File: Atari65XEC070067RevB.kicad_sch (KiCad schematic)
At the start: 338 parts, among them J1 SIO, J2 MONITOR, J5 JOY1, J6 JOY1, J7 DIN-7, J8 KEYBOARD, Q1 2N3904, Q2 2N3904, Q3 2N3904, Q4 2N3904, Q5 2N3904, Q6 2N3904, Q7 MPSA55, SW1 SW_SPDT, U1 LM358, U10 4164, U11 4164, U12 4164, U13 4164, U14 4164, U15 4164, U16 4164, U17 C014889/GTIA, U18 74LS08, U19 NE555P, U2 74LS138, U20 4050, U21 74LS74, U22 C012294/POKEY, U23 C014795 PIA/6520, U24 4051, U25 4051, U26 4164, U27 4164, U28 4164, U29 4164, U3 MMU, U30 4164, U31 4164, U32 4164, U33 4164, U34 MMMU, U35 74LS95, U4 BASIC, U5 OS ROM, U6 CO14806/SALLY, U7 C021698/ANTIC, U8 C061991/FREDDIE, U9 4164, Y2 4.33618MHz

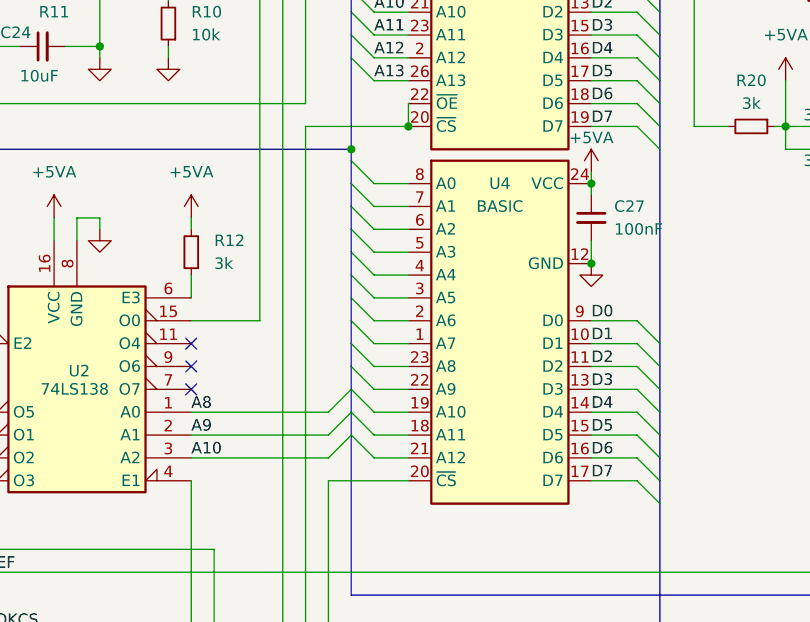
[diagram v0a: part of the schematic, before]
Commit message: fix ROM positions
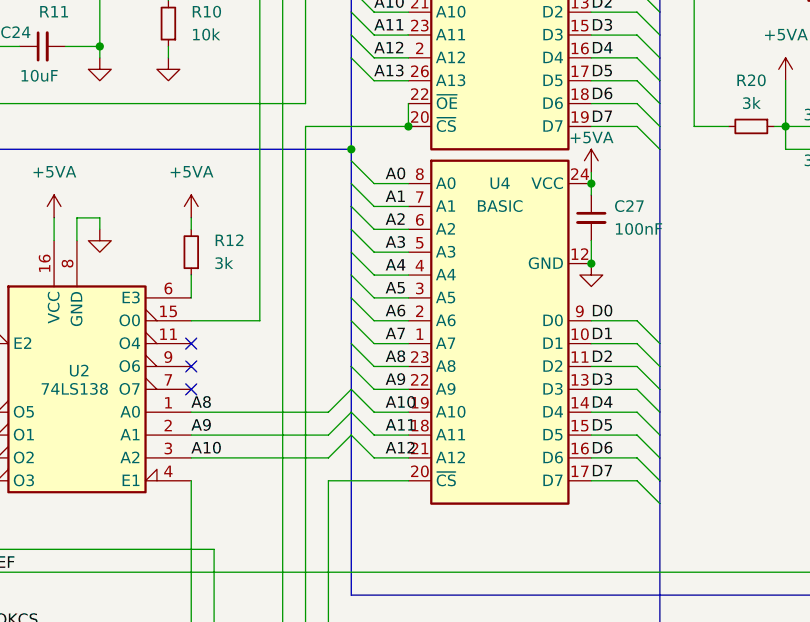
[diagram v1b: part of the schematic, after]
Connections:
- net A0: now also U4.8 (A0)
- net A1: now also U4.7 (A1)
- net A10: now also U4.19 (A10)
- net A11: now also U4.18 (A11)
- net A12: now also U4.21 (A12)
- net A2: now also U4.6 (A2)
- net A3: now also U4.5 (A3)
- net A4: now also U4.4 (A4)
- net A5: now also U4.3 (A5)
- net A6: now also U4.2 (A6)
- net A7: now also U4.1 (A7)
- net A8: now also U4.23 (A8)
- net A9: now also U4.22 (A9)
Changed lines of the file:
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@@
+		)
+	)
+	(label "A1"
+		(at 132.08 160.02 0)
+		(effects
+			(font
+				(size 1.27 1.27)
+			)
+			(justify left bottom)
 		)
 	)
@@
 		)
 	)
+	(label "A5"
+		(at 132.08 170.18 0)
+		(effects
+			(font
+				(size 1.27 1.27)
+			)
+			(justify left bottom)
+		)
+	)
 	(label "A4"
 		(at 203.2 95.25 0)
@@
 		)
 	)
+	(label "A3"
+		(at 132.08 165.1 0)
+		(effects
+			(font
+				(size 1.27 1.27)
+			)
+			(justify left bottom)
+		)
+	)
 	(label "D4"
 		(at 154.94 182.88 0)
@@
 		)
 	)
+	(label "A12"
+		(at 132.08 187.96 0)
+		(effects
+			(font
+				(size 1.27 1.27)
+			)
+			(justify left bottom)
+		)
+	)
 	(label "P2"
 		(at 461.01 351.79 0)
@@
 		)
 	)
+	(label "A10"
+		(at 132.08 182.88 0)
+		(effects
+			(font
+				(size 1.27 1.27)
+			)
+			(justify left bottom)
+		)
+	)
 	(label "D6"
 		(at 361.95 318.77 180)
@@
 		)
 	)
+	(label "A6"
+		(at 132.08 172.72 0)
+		(effects
+			(font
+				(size 1.27 1.27)
+			)
+			(justify left bottom)
+		)
+	)
 	(label "A12"
 		(at 130.81 143.51 0)
@@
 		)
 	)
+	(label "A0"
+		(at 132.08 157.48 0)
+		(effects
+			(font
+				(size 1.27 1.27)
+			)
+			(justify left bottom)
+		)
+	)
 	(label "PB7"
 		(at 85.09 228.6 0)
@@
 		)
 	)
+	(label "A2"
+		(at 132.08 162.56 0)
+		(effects
+			(font
+				(size 1.27 1.27)
+			)
+			(justify left bottom)
+		)
+	)
 	(label "A15"
 		(at 203.2 123.19 0)
@@
 		)
 	)
+	(label "A8"
+		(at 132.08 177.8 0)
+		(effects
+			(font
+				(size 1.27 1.27)
+			)
+			(justify left bottom)
+		)
+	)
 	(label "A0"
 		(at 130.81 113.03 0)
@@
 		)
 	)
+	(label "A7"
+		(at 132.08 175.26 0)
+		(effects
+			(font
+				(size 1.27 1.27)
+			)
+			(justify left bottom)
+		)
+	)
 	(label "S0"
 		(at 299.72 107.95 0)
@@
 		)
 	)
+	(label "A11"
+		(at 132.08 185.42 0)
+		(effects
+			(font
+				(size 1.27 1.27)
+			)
+			(justify left bottom)
+		)
+	)
 	(label "D5"
 		(at 285.75 259.08 0)
@@
 		)
 	)
+	(label "A9"
+		(at 132.08 180.34 0)
+		(effects
+			(font
+				(size 1.27 1.27)
+			)
+			(justify left bottom)
+		)
+	)
 	(label "A15"
 		(at 82.55 323.85 180)
@@
 		)
 	)
+	(label "A4"
+		(at 132.08 167.64 0)
+		(effects
+			(font
+				(size 1.27 1.27)
+			)
+			(justify left bottom)
+		)
+	)

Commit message: progress routing
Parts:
- L37: footprint Inductor_THT:L_Axial_L7.0mm_D3.3mm_P12.70mm_Horizontal_Fastron_MICC -> Library:R_Axial_L9.0mm_D2.7mm_P12.70mm_Horizontal
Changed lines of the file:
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@@
 			)
 		)
-		(property "Footprint" "Inductor_THT:L_Axial_L7.0mm_D3.3mm_P12.70mm_Horizontal_Fastron_MICC"
+		(property "Footprint" "Library:R_Axial_L9.0mm_D2.7mm_P12.70mm_Horizontal"
 			(at 247.65 228.6 0)
 			(effects

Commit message: fix phi2 wiring
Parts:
- L8: footprint Inductor_THT:L_Axial_L7.0mm_D3.3mm_P12.70mm_Horizontal_Fastron_MICC -> Library:R_Axial_L9.0mm_D2.7mm_P12.70mm_Horizontal
- renumbered R20 to R19, R19 to R20
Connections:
- net BO2: no longer U34.19 (O2), U8.5 (O2)
- net at Y2.1: now also C111.1, L8.1, R71.1; no longer C59.2
- net at U23.12 (PB2), U34.3 (BA14): now also R23.2; no longer R25.2
- net at U23.13 (PB3), U34.4 (BA15): now also R25.2; no longer R23.2
- net at R20.1, U18.1: now also U34.19 (O2), U6.39 (O2), U8.5 (O2)
- new net: C59.2, Y2.2
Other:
- moved on the sheet: R13, R20

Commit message: update fills and footprints
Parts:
- J8: footprint (none) -> Library:KEYBOARD
- Q1, Q2, Q3, Q4, Q5, Q6, Q7: footprint PCM_Package_TO_SOT_THT_AKL:TO-92_Inline_Wide_EBC -> Library:TO-92L_Inline_Wide
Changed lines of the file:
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@@
 			)
 		)
-		(property "Footprint" "PCM_Package_TO_SOT_THT_AKL:TO-92_Inline_Wide_EBC"
+		(property "Footprint" "Library:TO-92L_Inline_Wide"
 			(at 212.09 382.27 0)
 			(effects
@@
 			)
 		)
-		(property "Footprint" "PCM_Package_TO_SOT_THT_AKL:TO-92_Inline_Wide_EBC"
+		(property "Footprint" "Library:TO-92L_Inline_Wide"
 			(at 398.78 118.11 0)
 			(effects
@@
 			)
 		)
-		(property "Footprint" "PCM_Package_TO_SOT_THT_AKL:TO-92_Inline_Wide_EBC"
+		(property "Footprint" "Library:TO-92L_Inline_Wide"
 			(at 391.16 72.39 0)
 			(effects
@@
 			)
 		)
-		(property "Footprint" "PCM_Package_TO_SOT_THT_AKL:TO-92_Inline_Wide_EBC"
+		(property "Footprint" "Library:TO-92L_Inline_Wide"
 			(at 471.17 107.95 0)
 			(effects
@@
 			)
 		)
-		(property "Footprint" "PCM_Package_TO_SOT_THT_AKL:TO-92_Inline_Wide_EBC"
+		(property "Footprint" "Library:TO-92L_Inline_Wide"
 			(at 190.5 374.65 0)
 			(effects
@@
 			)
 		)
-		(property "Footprint" ""
+		(property "Footprint" "Library:KEYBOARD"
 			(at 497.84 309.88 0)
 			(effects
@@
 			)
 		)
-		(property "Footprint" "PCM_Package_TO_SOT_THT_AKL:TO-92_Inline_Wide_EBC"
+		(property "Footprint" "Library:TO-92L_Inline_Wide"
 			(at 355.6 153.67 0)
 			(effects
@@
 			)
 		)
-		(property "Footprint" "PCM_Package_TO_SOT_THT_AKL:TO-92_Inline_Wide_EBC"
+		(property "Footprint" "Library:TO-92L_Inline_Wide"
 			(at 283.21 171.45 0)
 			(effects

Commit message: refine board definition
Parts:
- added H1, H2: MountingHole, Library:Cutout, symbol Mechanical:MountingHole
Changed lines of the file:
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@@
 	)
 	(symbol
+		(lib_id "Mechanical:MountingHole")
+		(at 17.78 363.22 0)
+		(unit 1)
+		(exclude_from_sim yes)
+		(in_bom no)
+		(on_board yes)
+		(dnp no)
+		(fields_autoplaced yes)
+		(property "Reference" "H1"
+			(at 20.32 361.9499 0)
+			(effects
+				(font
+					(size 1.27 1.27)
+				)
+				(justify left)
+			)
+		)
+		(property "Value" "MountingHole"
+			(at 20.32 364.4899 0)
+			(effects
+				(font
+					(size 1.27 1.27)
+				)
+				(justify left)
+			)
+		)
+		(property "Footprint" "Library:Cutout"
+			(at 17.78 363.22 0)
+			(effects
+				(font
+					(size 1.27 1.27)
+				)
+				(hide yes)
+			)
+		)
+		(property "Datasheet" "~"
+			(at 17.78 363.22 0)
+			(effects
+				(font
+					(size 1.27 1.27)
+				)
+				(hide yes)
+			)
+		)
+		(property "Description" "Mounting Hole without connection"
+			(at 17.78 363.22 0)
+			(effects
+				(font
+					(size 1.27 1.27)
+				)
+				(hide yes)
+			)
+		)
+		(instances
+			(project ""
+				(path "/87d66ada-8337-4a7e-bc00-d889029d79b8"
+					(reference "H1")
+					(unit 1)
+				)
+			)
+		)
+	)
+	(symbol
 		(lib_id "power:GND")
 		(at 237.49 317.5 0)
@@
 					(unit 1)
 				)
+			)
+		)
+	)
+	(symbol
+		(lib_id "Mechanical:MountingHole")
+		(at 17.78 369.57 0)
+		(unit 1)
+		(exclude_from_sim yes)
+		(in_bom no)
+		(on_board yes)
+		(dnp no)
+		(fields_autoplaced yes)
+		(property "Reference" "H2"
+			(at 20.32 368.2999 0)
+			(effects
+				(font
+					(size 1.27 1.27)
+				)
+				(justify left)
+			)
+		)
+		(property "Value" "MountingHole"
+			(at 20.32 370.8399 0)
+			(effects
+				(font
+					(size 1.27 1.27)
+				)
+				(justify left)
+			)
+		)
+		(property "Footprint" "Library:Cutout"
+			(at 17.78 369.57 0)
+			(effects
+				(font
+					(size 1.27 1.27)
+				)
+				(hide yes)
+			)
+		)
+		(property "Datasheet" "~"
+			(at 17.78 369.57 0)
+			(effects
+				(font
+					(size 1.27 1.27)
+				)
+				(hide yes)
+			)
+		)
+		(property "Description" "Mounting Hole without connection"
+			(at 17.78 369.57 0)
+			(effects
+				(font
+					(size 1.27 1.27)
+				)
+				(hide yes)
+			)
+		)
+		(instances
+			(project "Atari65XEC070067RevB"
+				(path "/87d66ada-8337-4a7e-bc00-d889029d79b8"
+					(reference "H2")
+					(unit 1)
+				)

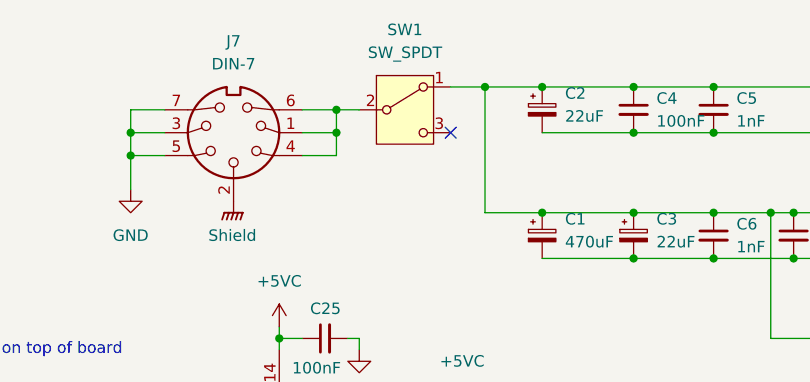
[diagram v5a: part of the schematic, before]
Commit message: place power circuit components
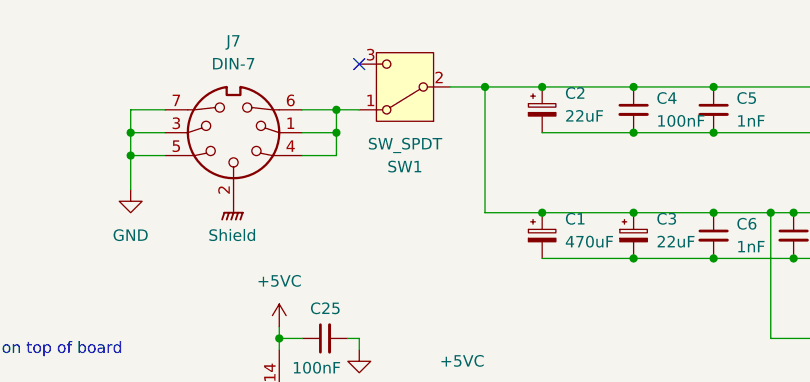
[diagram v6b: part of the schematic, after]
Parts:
- C1: footprint Capacitor_THT:CP_Radial_D8.0mm_P5.00mm -> Capacitor_THT:CP_Radial_D10.0mm_P5.00mm
- C10, C2, C3: footprint Capacitor_THT:CP_Radial_D8.0mm_P5.00mm -> Capacitor_THT:CP_Axial_L11.0mm_D5.0mm_P18.00mm_Horizontal
- J7: footprint (none) -> Library:CUI_SDS-70J
- L1, L2, L3: footprint Inductor_THT:L_Axial_L7.0mm_D3.3mm_P12.70mm_Horizontal_Fastron_MICC -> Library:R_Axial_L9.0mm_D2.7mm_P12.70mm_Horizontal
- SW1: footprint (none) -> Library:PowerSwitch
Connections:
- net at C1.1, C2.1, C3.1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: now also SW1.2 (B); no longer SW1.1 (A)
- net at J7.1, J7.4, J7.6: now also SW1.1 (A); no longer SW1.2 (B)
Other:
- moved on the sheet: SW1
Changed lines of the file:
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@@
 	)
 	(no_connect
-		(at 88.9 27.94)
+		(at 78.74 20.32)
 	)
 	(no_connect
@@
 			)
 		)
-		(property "Footprint" "Capacitor_THT:CP_Radial_D8.0mm_P5.00mm"
+		(property "Footprint" "Capacitor_THT:CP_Axial_L11.0mm_D5.0mm_P18.00mm_Horizontal"
 			(at 109.22 39.37 0)
 			(effects
@@
 			)
 		)
-		(property "Footprint" "Inductor_THT:L_Axial_L7.0mm_D3.3mm_P12.70mm_Horizontal_Fastron_MICC"
+		(property "Footprint" "Library:R_Axial_L9.0mm_D2.7mm_P12.70mm_Horizontal"
 			(at 133.35 22.86 0)
 			(effects
@@
 			)
 		)
-		(property "Footprint" "Capacitor_THT:CP_Radial_D8.0mm_P5.00mm"
+		(property "Footprint" "Capacitor_THT:CP_Radial_D10.0mm_P5.00mm"
 			(at 99.06 39.37 0)
 			(effects
@@
 			)
 		)
-		(property "Footprint" "Capacitor_THT:CP_Radial_D8.0mm_P5.00mm"
+		(property "Footprint" "Capacitor_THT:CP_Axial_L11.0mm_D5.0mm_P18.00mm_Horizontal"
 			(at 142.24 53.34 0)
 			(effects
@@
 			)
 		)
-		(property "Footprint" "Inductor_THT:L_Axial_L7.0mm_D3.3mm_P12.70mm_Horizontal_Fastron_MICC"
+		(property "Footprint" "Library:R_Axial_L9.0mm_D2.7mm_P12.70mm_Horizontal"
 			(at 133.35 50.8 0)
 			(effects
@@
 	(symbol
 		(lib_id "Switch:SW_SPDT")
-		(at 83.82 25.4 0)
+		(at 83.82 22.86 180)
 		(unit 1)
 		(exclude_from_sim no)
@@
 		(fields_autoplaced yes)
 		(property "Reference" "SW1"
-			(at 83.82 16.51 0)
+			(at 83.82 31.75 0)
 			(effects
 				(font
@@
 		)
 		(property "Value" "SW_SPDT"
-			(at 83.82 19.05 0)
+			(at 83.82 29.21 0)
 			(effects
 				(font
@@
 			)
 		)
-		(property "Footprint" ""
-			(at 83.82 25.4 0)
+		(property "Footprint" "Library:PowerSwitch"
+			(at 83.82 22.86 0)
 			(effects
 				(font
@@
 		)
 		(property "Datasheet" "~"
-			(at 83.82 33.02 0)
+			(at 83.82 15.24 0)
 			(effects
 				(font
@@
 		)
 		(property "Description" "Switch, single pole double throw"
-			(at 83.82 25.4 0)
+			(at 83.82 22.86 0)
 			(effects
 				(font
@@
 			)
 		)
-		(property "Footprint" ""
+		(property "Footprint" "Library:CUI_SDS-70J"
 			(at 64.77 27.94 0)
 			(effects
@@
 			)
 		)
-		(property "Footprint" "Inductor_THT:L_Axial_L7.0mm_D3.3mm_P12.70mm_Horizontal_Fastron_MICC"
+		(property "Footprint" "Library:R_Axial_L9.0mm_D2.7mm_P12.70mm_Horizontal"
 			(at 133.35 36.83 0)
 			(effects
@@
 			)
 		)
-		(property "Footprint" "Capacitor_THT:CP_Radial_D8.0mm_P5.00mm"
+		(property "Footprint" "Capacitor_THT:CP_Axial_L11.0mm_D5.0mm_P18.00mm_Horizontal"
 			(at 99.06 25.4 0)
 			(effects

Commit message: revise ram chip positions
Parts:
- C113, C114, C115, C116, C117, C118, C119, C120, C34, C35, C36, C37, C38, C39, C40, C41: footprint Library:C_Axial_L3.8mm_D2.6mm_P10.16mm_Horizontal -> Library:C_Axial_L3.8mm_D2.6mm_P8.89mm_Horizontal
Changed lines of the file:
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@@
 			)
 		)
-		(property "Footprint" "Library:C_Axial_L3.8mm_D2.6mm_P10.16mm_Horizontal"
+		(property "Footprint" "Library:C_Axial_L3.8mm_D2.6mm_P8.89mm_Horizontal"
 			(at 214.63 313.69 0)
 			(effects
@@
 			)
 		)
-		(property "Footprint" "Library:C_Axial_L3.8mm_D2.6mm_P10.16mm_Horizontal"
+		(property "Footprint" "Library:C_Axial_L3.8mm_D2.6mm_P8.89mm_Horizontal"
 			(at 285.75 313.69 0)
 			(effects
@@
 			)
 		)
-		(property "Footprint" "Library:C_Axial_L3.8mm_D2.6mm_P10.16mm_Horizontal"
+		(property "Footprint" "Library:C_Axial_L3.8mm_D2.6mm_P8.89mm_Horizontal"
 			(at 207.01 313.69 0)
 			(effects
@@
 			)
 		)
-		(property "Footprint" "Library:C_Axial_L3.8mm_D2.6mm_P10.16mm_Horizontal"
+		(property "Footprint" "Library:C_Axial_L3.8mm_D2.6mm_P8.89mm_Horizontal"
 			(at 184.15 313.69 0)
 			(effects
@@
 			)
 		)
-		(property "Footprint" "Library:C_Axial_L3.8mm_D2.6mm_P10.16mm_Horizontal"
+		(property "Footprint" "Library:C_Axial_L3.8mm_D2.6mm_P8.89mm_Horizontal"
 			(at 270.51 313.69 0)
 			(effects
@@
 			)
 		)
-		(property "Footprint" "Library:C_Axial_L3.8mm_D2.6mm_P10.16mm_Horizontal"
+		(property "Footprint" "Library:C_Axial_L3.8mm_D2.6mm_P8.89mm_Horizontal"
 			(at 278.13 313.69 0)
 			(effects
@@
 			)
 		)
-		(property "Footprint" "Library:C_Axial_L3.8mm_D2.6mm_P10.16mm_Horizontal"
+		(property "Footprint" "Library:C_Axial_L3.8mm_D2.6mm_P8.89mm_Horizontal"
 			(at 191.77 313.69 0)
 			(effects
@@
 			)
 		)
-		(property "Footprint" "Library:C_Axial_L3.8mm_D2.6mm_P10.16mm_Horizontal"
+		(property "Footprint" "Library:C_Axial_L3.8mm_D2.6mm_P8.89mm_Horizontal"
 			(at 293.37 313.69 0)
 			(effects
@@
 			)
 		)
-		(property "Footprint" "Library:C_Axial_L3.8mm_D2.6mm_P10.16mm_Horizontal"
+		(property "Footprint" "Library:C_Axial_L3.8mm_D2.6mm_P8.89mm_Horizontal"
 			(at 262.89 313.69 0)
 			(effects
@@
 			)
 		)
-		(property "Footprint" "Library:C_Axial_L3.8mm_D2.6mm_P10.16mm_Horizontal"
+		(property "Footprint" "Library:C_Axial_L3.8mm_D2.6mm_P8.89mm_Horizontal"
 			(at 199.39 313.69 0)
 			(effects
@@
 			)
 		)
-		(property "Footprint" "Library:C_Axial_L3.8mm_D2.6mm_P10.16mm_Horizontal"
+		(property "Footprint" "Library:C_Axial_L3.8mm_D2.6mm_P8.89mm_Horizontal"
 			(at 247.65 313.69 0)
 			(effects
@@
 			)
 		)
-		(property "Footprint" "Library:C_Axial_L3.8mm_D2.6mm_P10.16mm_Horizontal"
+		(property "Footprint" "Library:C_Axial_L3.8mm_D2.6mm_P8.89mm_Horizontal"
 			(at 237.49 313.69 0)
 			(effects
@@
 			)
 		)
-		(property "Footprint" "Library:C_Axial_L3.8mm_D2.6mm_P10.16mm_Horizontal"
+		(property "Footprint" "Library:C_Axial_L3.8mm_D2.6mm_P8.89mm_Horizontal"
 			(at 255.27 313.69 0)
 			(effects
@@
 			)
 		)
-		(property "Footprint" "Library:C_Axial_L3.8mm_D2.6mm_P10.16mm_Horizontal"
+		(property "Footprint" "Library:C_Axial_L3.8mm_D2.6mm_P8.89mm_Horizontal"
 			(at 300.99 313.69 0)
 			(effects
@@
 			)
 		)
-		(property "Footprint" "Library:C_Axial_L3.8mm_D2.6mm_P10.16mm_Horizontal"
+		(property "Footprint" "Library:C_Axial_L3.8mm_D2.6mm_P8.89mm_Horizontal"
 			(at 229.87 313.69 0)
 			(effects
@@
 			)
 		)
-		(property "Footprint" "Library:C_Axial_L3.8mm_D2.6mm_P10.16mm_Horizontal"
+		(property "Footprint" "Library:C_Axial_L3.8mm_D2.6mm_P8.89mm_Horizontal"
 			(at 222.25 313.69 0)
 			(effects
